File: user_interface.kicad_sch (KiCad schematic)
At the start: 33 parts, among them J3 Внутр. коннектор потенциометр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, J4 Внутр. коннектор галлетника (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, SW1 Кнопка тактовая 6x6 без фикса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, SW2 Кнопка тактовая 6x6 без фикса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, SW3 Кнопка тактовая 6x6 без фикса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, SW4 Кнопка тактовая 6x6 без фикса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, SW5 Кнопка тактовая 6x6 без фикса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, SW6 Кнопка тактовая 6x6 без фикса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

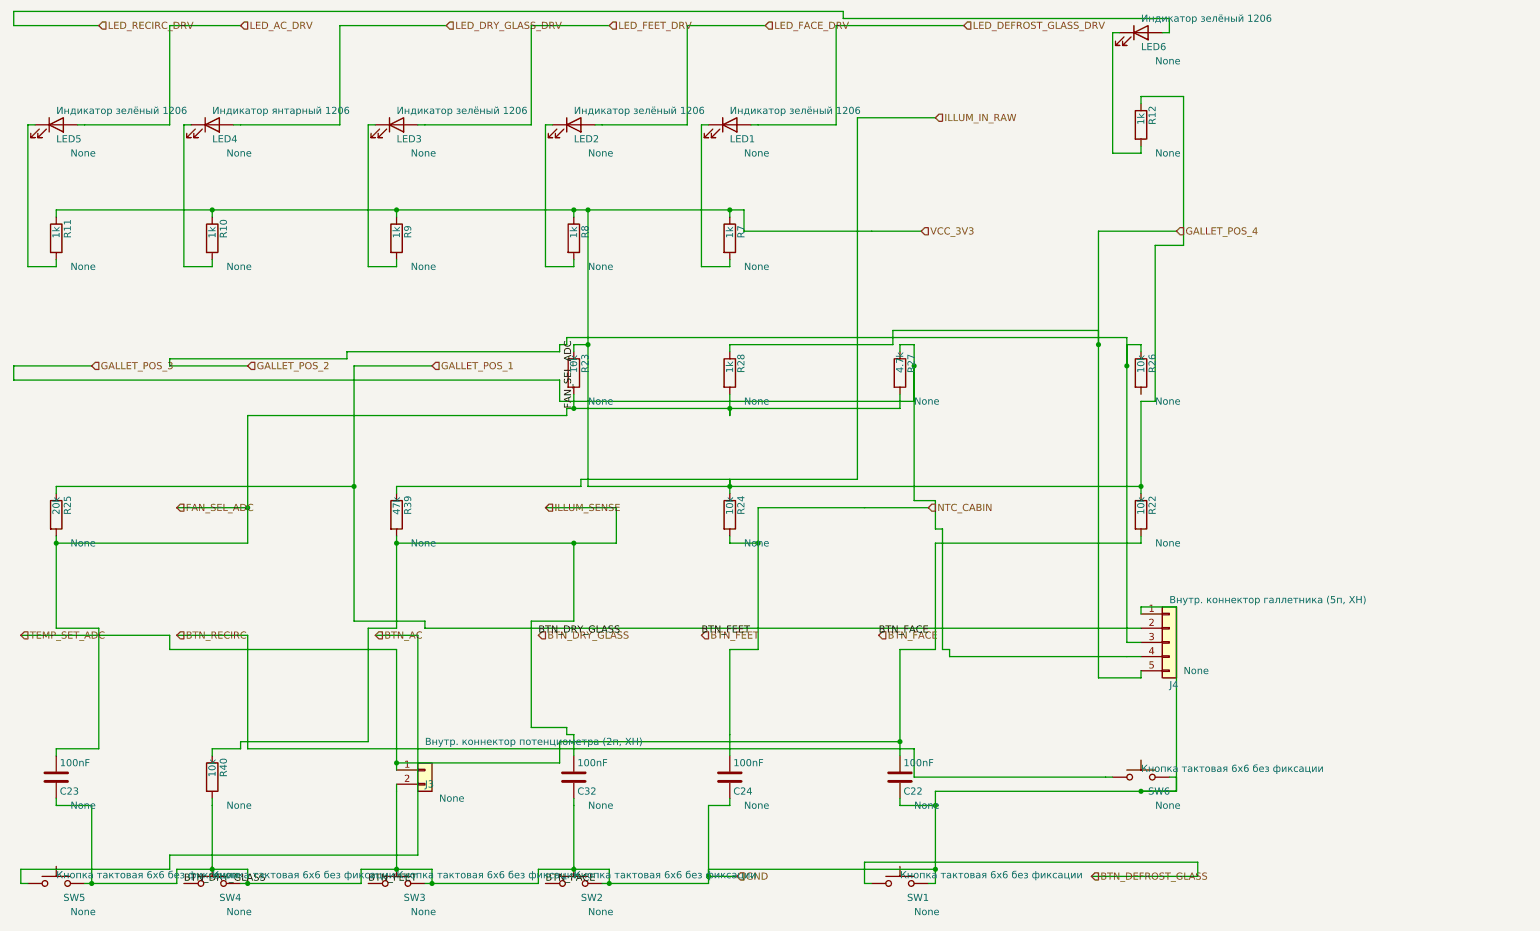
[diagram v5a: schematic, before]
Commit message: реализована 2я занятость клетки
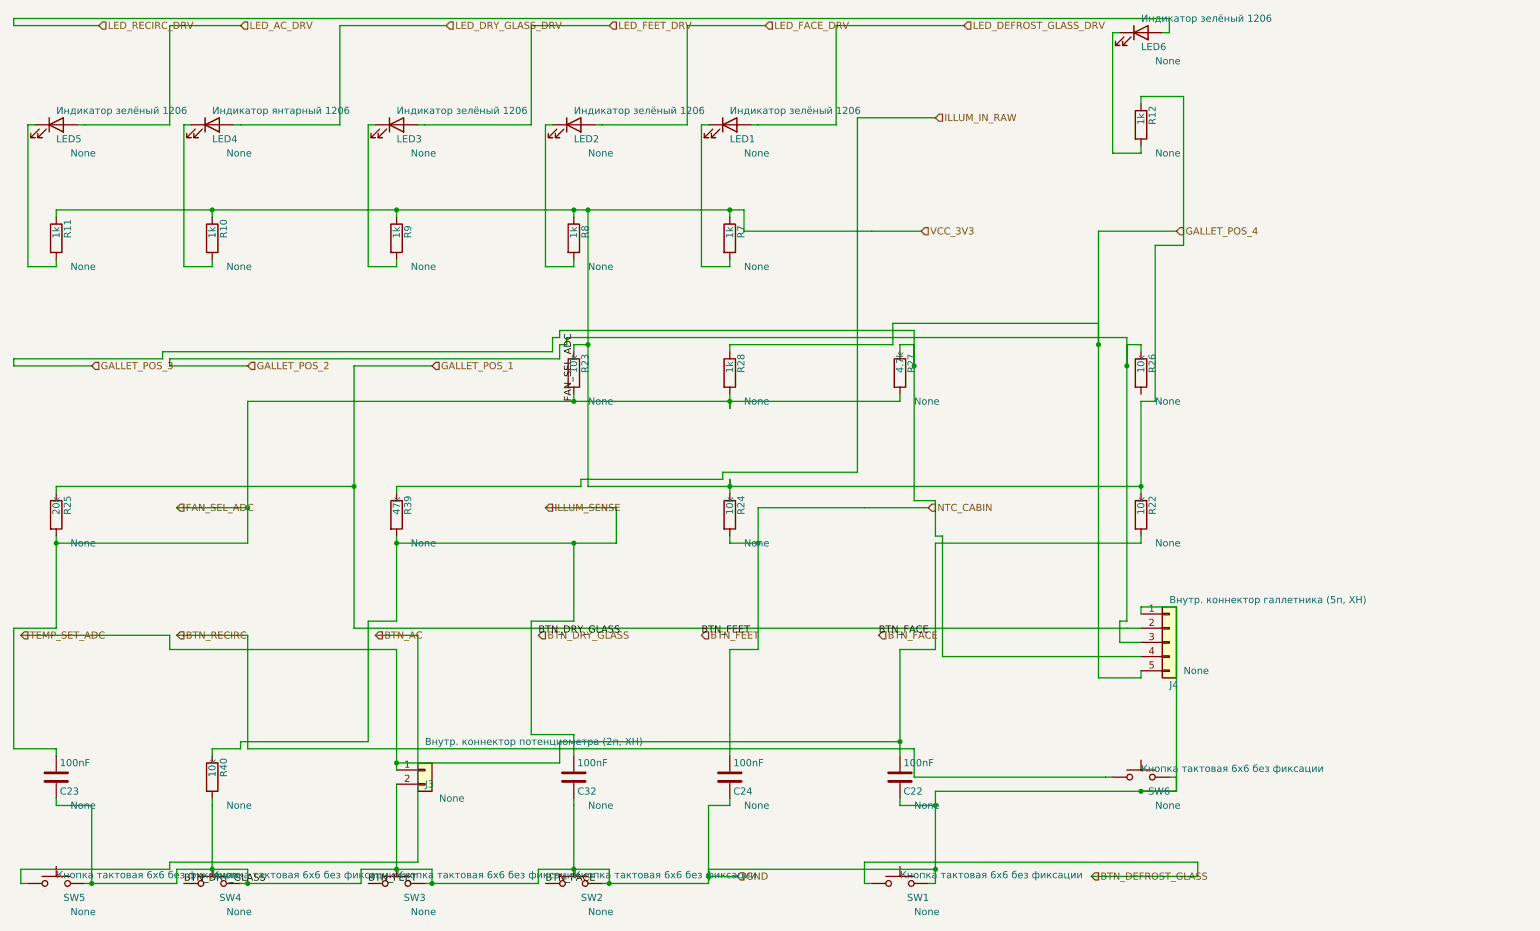
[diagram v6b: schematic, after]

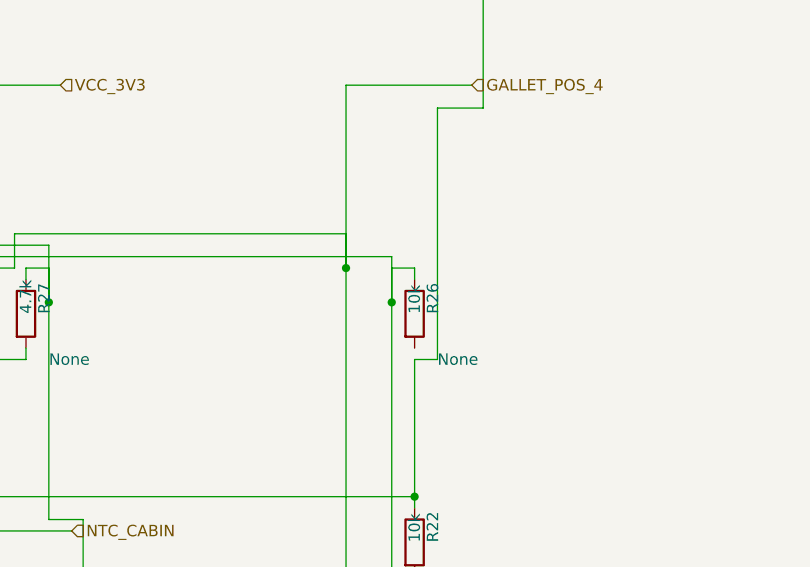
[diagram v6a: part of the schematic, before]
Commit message: фильтр клеток для Т если там пересечение
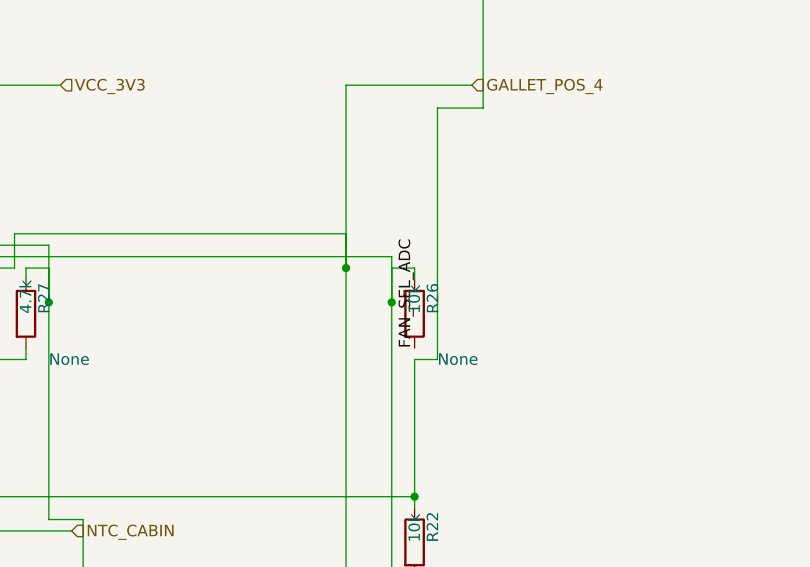
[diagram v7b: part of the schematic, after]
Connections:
- net FAN_SEL_ADC: now also R26.2
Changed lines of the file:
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@@
 		(instances
 			(project "Untitled"
-				(path "/80450f1d-307b-487e-a667-f10d610ada31"
+				(path "/5dda3bb2-7169-4d21-8754-437af9eafa82"
 					(reference "C22")
 					(unit 1)
@@
 		(instances
 			(project "Untitled"
-				(path "/80450f1d-307b-487e-a667-f10d610ada31"
+				(path "/5dda3bb2-7169-4d21-8754-437af9eafa82"
 					(reference "C23")
 					(unit 1)
@@
 		(instances
 			(project "Untitled"
-				(path "/80450f1d-307b-487e-a667-f10d610ada31"
+				(path "/5dda3bb2-7169-4d21-8754-437af9eafa82"
 					(reference "C24")
 					(unit 1)
@@
 		(instances
 			(project "Untitled"
-				(path "/80450f1d-307b-487e-a667-f10d610ada31"
+				(path "/5dda3bb2-7169-4d21-8754-437af9eafa82"
 					(reference "C32")
 					(unit 1)
@@
 		(instances
 			(project "Untitled"
-				(path "/80450f1d-307b-487e-a667-f10d610ada31"
+				(path "/5dda3bb2-7169-4d21-8754-437af9eafa82"
 					(reference "J3")
 					(unit 1)
@@
 		(instances
 			(project "Untitled"
-				(path "/80450f1d-307b-487e-a667-f10d610ada31"
+				(path "/5dda3bb2-7169-4d21-8754-437af9eafa82"
 					(reference "J4")
 					(unit 1)
@@
 		(instances
 			(project "Untitled"
-				(path "/80450f1d-307b-487e-a667-f10d610ada31"
+				(path "/5dda3bb2-7169-4d21-8754-437af9eafa82"
 					(reference "LED1")
 					(unit 1)
@@
 		(instances
 			(project "Untitled"
-				(path "/80450f1d-307b-487e-a667-f10d610ada31"
+				(path "/5dda3bb2-7169-4d21-8754-437af9eafa82"
 					(reference "LED2")
 					(unit 1)
@@
 		(instances
 			(project "Untitled"
-				(path "/80450f1d-307b-487e-a667-f10d610ada31"
+				(path "/5dda3bb2-7169-4d21-8754-437af9eafa82"
 					(reference "LED3")
 					(unit 1)
@@
 		(instances
 			(project "Untitled"
-				(path "/80450f1d-307b-487e-a667-f10d610ada31"
+				(path "/5dda3bb2-7169-4d21-8754-437af9eafa82"
 					(reference "LED4")
 					(unit 1)
@@
 		(instances
 			(project "Untitled"
-				(path "/80450f1d-307b-487e-a667-f10d610ada31"
+				(path "/5dda3bb2-7169-4d21-8754-437af9eafa82"
 					(reference "LED5")
 					(unit 1)
@@
 		(instances
 			(project "Untitled"
-				(path "/80450f1d-307b-487e-a667-f10d610ada31"
+				(path "/5dda3bb2-7169-4d21-8754-437af9eafa82"
 					(reference "LED6")
 					(unit 1)
@@
 		(instances
 			(project "Untitled"
-				(path "/80450f1d-307b-487e-a667-f10d610ada31"
+				(path "/5dda3bb2-7169-4d21-8754-437af9eafa82"
 					(reference "R7")
 					(unit 1)
@@
 		(instances
 			(project "Untitled"
-				(path "/80450f1d-307b-487e-a667-f10d610ada31"
+				(path "/5dda3bb2-7169-4d21-8754-437af9eafa82"
 					(reference "R8")
 					(unit 1)
@@
 		(instances
 			(project "Untitled"
-				(path "/80450f1d-307b-487e-a667-f10d610ada31"
+				(path "/5dda3bb2-7169-4d21-8754-437af9eafa82"
 					(reference "R9")
 					(unit 1)
@@
 		(instances
 			(project "Untitled"
-				(path "/80450f1d-307b-487e-a667-f10d610ada31"
+				(path "/5dda3bb2-7169-4d21-8754-437af9eafa82"
 					(reference "R10")
 					(unit 1)
@@
 		(instances
 			(project "Untitled"
-				(path "/80450f1d-307b-487e-a667-f10d610ada31"
+				(path "/5dda3bb2-7169-4d21-8754-437af9eafa82"
 					(reference "R11")
 					(unit 1)
@@
 		(instances
 			(project "Untitled"
-				(path "/80450f1d-307b-487e-a667-f10d610ada31"
+				(path "/5dda3bb2-7169-4d21-8754-437af9eafa82"
 					(reference "R12")
 					(unit 1)
@@
 		(instances
 			(project "Untitled"
-				(path "/80450f1d-307b-487e-a667-f10d610ada31"
+				(path "/5dda3bb2-7169-4d21-8754-437af9eafa82"
 					(reference "R22")
 					(unit 1)
@@
 		(instances
 			(project "Untitled"
-				(path "/80450f1d-307b-487e-a667-f10d610ada31"
+				(path "/5dda3bb2-7169-4d21-8754-437af9eafa82"
 					(reference "R23")
 					(unit 1)
@@
 		(instances
 			(project "Untitled"
-				(path "/80450f1d-307b-487e-a667-f10d610ada31"
+				(path "/5dda3bb2-7169-4d21-8754-437af9eafa82"
 					(reference "R24")
 					(unit 1)
@@
 		(instances
 			(project "Untitled"
-				(path "/80450f1d-307b-487e-a667-f10d610ada31"
+				(path "/5dda3bb2-7169-4d21-8754-437af9eafa82"
 					(reference "R39")
 					(unit 1)
@@
 		(instances
 			(project "Untitled"
-				(path "/80450f1d-307b-487e-a667-f10d610ada31"
+				(path "/5dda3bb2-7169-4d21-8754-437af9eafa82"
 					(reference "R40")
 					(unit 1)
@@
 		(instances
 			(project "Untitled"
-				(path "/80450f1d-307b-487e-a667-f10d610ada31"
+				(path "/5dda3bb2-7169-4d21-8754-437af9eafa82"
 					(reference "R25")
 					(unit 1)
@@
 		(instances
 			(project "Untitled"
-				(path "/80450f1d-307b-487e-a667-f10d610ada31"
+				(path "/5dda3bb2-7169-4d21-8754-437af9eafa82"
 					(reference "R26")
 					(unit 1)
@@
 		(instances
 			(project "Untitled"
-				(path "/80450f1d-307b-487e-a667-f10d610ada31"
+				(path "/5dda3bb2-7169-4d21-8754-437af9eafa82"
 					(reference "R27")
 					(unit 1)
@@
 		(instances
 			(project "Untitled"
-				(path "/80450f1d-307b-487e-a667-f10d610ada31"
+				(path "/5dda3bb2-7169-4d21-8754-437af9eafa82"
 					(reference "R28")
 					(unit 1)
@@
 		(instances
 			(project "Untitled"
-				(path "/80450f1d-307b-487e-a667-f10d610ada31"
+				(path "/5dda3bb2-7169-4d21-8754-437af9eafa82"
 					(reference "SW1")
 					(unit 1)
@@
 		(instances
 			(project "Untitled"
-				(path "/80450f1d-307b-487e-a667-f10d610ada31"
+				(path "/5dda3bb2-7169-4d21-8754-437af9eafa82"
 					(reference "SW2")
 					(unit 1)
@@
 		(instances
 			(project "Untitled"
-				(path "/80450f1d-307b-487e-a667-f10d610ada31"
+				(path "/5dda3bb2-7169-4d21-8754-437af9eafa82"
 					(reference "SW3")
 					(unit 1)
@@
 		(instances
 			(project "Untitled"
-				(path "/80450f1d-307b-487e-a667-f10d610ada31"
+				(path "/5dda3bb2-7169-4d21-8754-437af9eafa82"
 					(reference "SW4")
 					(unit 1)
@@
 		(instances
 			(project "Untitled"
-				(path "/80450f1d-307b-487e-a667-f10d610ada31"
+				(path "/5dda3bb2-7169-4d21-8754-437af9eafa82"
 					(reference "SW5")
 					(unit 1)
@@
 		(instances
 			(project "Untitled"
-				(path "/80450f1d-307b-487e-a667-f10d610ada31"
+				(path "/5dda3bb2-7169-4d21-8754-437af9eafa82"
 					(reference "SW6")
 					(unit 1)
@@
 		(effects
 			(font
+				(size 1.27 1.27)
+			)
+			(justify left bottom)
+		)
+	)
+	(label "FAN_SEL_ADC"
+		(at 204.47 69.85 270)
+		(effects
+			(font

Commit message: fic placer for small schemes
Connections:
- net LED_FACE_A: now reaches LED2.1 (K), R8.2
- net LED_FEET_A: now reaches LED3.1 (K), R9.2
- net LED_DEFROST_GLASS_A: now reaches LED1.1 (K), R7.2
- net LED_DRY_GLASS_A: now reaches LED4.1 (K), R10.2
- net LED_RECIRC_A: now reaches LED6.1 (K), R12.2
- net LED_AC_A: now reaches LED5.1 (K), R11.2
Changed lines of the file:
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@@
 		(instances
 			(project "Untitled"
-				(path "/5dda3bb2-7169-4d21-8754-437af9eafa82"
+				(path "/f6aca846-33e6-4903-9ab4-0f8f6bf1ede3"
 					(reference "C22")
 					(unit 1)
@@
 		(instances
 			(project "Untitled"
-				(path "/5dda3bb2-7169-4d21-8754-437af9eafa82"
+				(path "/f6aca846-33e6-4903-9ab4-0f8f6bf1ede3"
 					(reference "C23")
 					(unit 1)
@@
 		(instances
 			(project "Untitled"
-				(path "/5dda3bb2-7169-4d21-8754-437af9eafa82"
+				(path "/f6aca846-33e6-4903-9ab4-0f8f6bf1ede3"
 					(reference "C24")
 					(unit 1)
@@
 		(instances
 			(project "Untitled"
-				(path "/5dda3bb2-7169-4d21-8754-437af9eafa82"
+				(path "/f6aca846-33e6-4903-9ab4-0f8f6bf1ede3"
 					(reference "C32")
 					(unit 1)
@@
 		(instances
 			(project "Untitled"
-				(path "/5dda3bb2-7169-4d21-8754-437af9eafa82"
+				(path "/f6aca846-33e6-4903-9ab4-0f8f6bf1ede3"
 					(reference "J3")
 					(unit 1)
@@
 		(instances
 			(project "Untitled"
-				(path "/5dda3bb2-7169-4d21-8754-437af9eafa82"
+				(path "/f6aca846-33e6-4903-9ab4-0f8f6bf1ede3"
 					(reference "J4")
 					(unit 1)
@@
 		(instances
 			(project "Untitled"
-				(path "/5dda3bb2-7169-4d21-8754-437af9eafa82"
+				(path "/f6aca846-33e6-4903-9ab4-0f8f6bf1ede3"
 					(reference "LED1")
 					(unit 1)
@@
 		(instances
 			(project "Untitled"
-				(path "/5dda3bb2-7169-4d21-8754-437af9eafa82"
+				(path "/f6aca846-33e6-4903-9ab4-0f8f6bf1ede3"
 					(reference "LED2")
 					(unit 1)
@@
 		(instances
 			(project "Untitled"
-				(path "/5dda3bb2-7169-4d21-8754-437af9eafa82"
+				(path "/f6aca846-33e6-4903-9ab4-0f8f6bf1ede3"
 					(reference "LED3")
 					(unit 1)
@@
 		(instances
 			(project "Untitled"
-				(path "/5dda3bb2-7169-4d21-8754-437af9eafa82"
+				(path "/f6aca846-33e6-4903-9ab4-0f8f6bf1ede3"
 					(reference "LED4")
 					(unit 1)
@@
 		(instances
 			(project "Untitled"
-				(path "/5dda3bb2-7169-4d21-8754-437af9eafa82"
+				(path "/f6aca846-33e6-4903-9ab4-0f8f6bf1ede3"
 					(reference "LED5")
 					(unit 1)
@@
 		(instances
 			(project "Untitled"
-				(path "/5dda3bb2-7169-4d21-8754-437af9eafa82"
+				(path "/f6aca846-33e6-4903-9ab4-0f8f6bf1ede3"
 					(reference "LED6")
 					(unit 1)
@@
 		(instances
 			(project "Untitled"
-				(path "/5dda3bb2-7169-4d21-8754-437af9eafa82"
+				(path "/f6aca846-33e6-4903-9ab4-0f8f6bf1ede3"
 					(reference "R7")
 					(unit 1)
@@
 		(instances
 			(project "Untitled"
-				(path "/5dda3bb2-7169-4d21-8754-437af9eafa82"
+				(path "/f6aca846-33e6-4903-9ab4-0f8f6bf1ede3"
 					(reference "R8")
 					(unit 1)
@@
 		(instances
 			(project "Untitled"
-				(path "/5dda3bb2-7169-4d21-8754-437af9eafa82"
+				(path "/f6aca846-33e6-4903-9ab4-0f8f6bf1ede3"
 					(reference "R9")
 					(unit 1)
@@
 		(instances
 			(project "Untitled"
-				(path "/5dda3bb2-7169-4d21-8754-437af9eafa82"
+				(path "/f6aca846-33e6-4903-9ab4-0f8f6bf1ede3"
 					(reference "R10")
 					(unit 1)
@@
 		(instances
 			(project "Untitled"
-				(path "/5dda3bb2-7169-4d21-8754-437af9eafa82"
+				(path "/f6aca846-33e6-4903-9ab4-0f8f6bf1ede3"
 					(reference "R11")
 					(unit 1)
@@
 		(instances
 			(project "Untitled"
-				(path "/5dda3bb2-7169-4d21-8754-437af9eafa82"
+				(path "/f6aca846-33e6-4903-9ab4-0f8f6bf1ede3"
 					(reference "R12")
 					(unit 1)
@@
 		(instances
 			(project "Untitled"
-				(path "/5dda3bb2-7169-4d21-8754-437af9eafa82"
+				(path "/f6aca846-33e6-4903-9ab4-0f8f6bf1ede3"
 					(reference "R22")
 					(unit 1)
@@
 		(instances
 			(project "Untitled"
-				(path "/5dda3bb2-7169-4d21-8754-437af9eafa82"
+				(path "/f6aca846-33e6-4903-9ab4-0f8f6bf1ede3"
 					(reference "R23")
 					(unit 1)
@@
 		(instances
 			(project "Untitled"
-				(path "/5dda3bb2-7169-4d21-8754-437af9eafa82"
+				(path "/f6aca846-33e6-4903-9ab4-0f8f6bf1ede3"
 					(reference "R24")
 					(unit 1)
@@
 		(instances
 			(project "Untitled"
-				(path "/5dda3bb2-7169-4d21-8754-437af9eafa82"
+				(path "/f6aca846-33e6-4903-9ab4-0f8f6bf1ede3"
 					(reference "R39")
 					(unit 1)
@@
 		(instances
 			(project "Untitled"
-				(path "/5dda3bb2-7169-4d21-8754-437af9eafa82"
+				(path "/f6aca846-33e6-4903-9ab4-0f8f6bf1ede3"
 					(reference "R40")
 					(unit 1)
@@
 		(instances
 			(project "Untitled"
-				(path "/5dda3bb2-7169-4d21-8754-437af9eafa82"
+				(path "/f6aca846-33e6-4903-9ab4-0f8f6bf1ede3"
 					(reference "R25")
 					(unit 1)
@@
 		(instances
 			(project "Untitled"
-				(path "/5dda3bb2-7169-4d21-8754-437af9eafa82"
+				(path "/f6aca846-33e6-4903-9ab4-0f8f6bf1ede3"
 					(reference "R26")
 					(unit 1)
@@
 		(instances
 			(project "Untitled"
-				(path "/5dda3bb2-7169-4d21-8754-437af9eafa82"
+				(path "/f6aca846-33e6-4903-9ab4-0f8f6bf1ede3"
 					(reference "R27")
 					(unit 1)
@@
 		(instances
 			(project "Untitled"
-				(path "/5dda3bb2-7169-4d21-8754-437af9eafa82"
+				(path "/f6aca846-33e6-4903-9ab4-0f8f6bf1ede3"
 					(reference "R28")
 					(unit 1)
@@
 		(instances
 			(project "Untitled"
-				(path "/5dda3bb2-7169-4d21-8754-437af9eafa82"
+				(path "/f6aca846-33e6-4903-9ab4-0f8f6bf1ede3"
 					(reference "SW1")
 					(unit 1)
@@
 		(instances
 			(project "Untitled"
-				(path "/5dda3bb2-7169-4d21-8754-437af9eafa82"
+				(path "/f6aca846-33e6-4903-9ab4-0f8f6bf1ede3"
 					(reference "SW2")
 					(unit 1)
@@
 		(instances
 			(project "Untitled"
-				(path "/5dda3bb2-7169-4d21-8754-437af9eafa82"
+				(path "/f6aca846-33e6-4903-9ab4-0f8f6bf1ede3"
 					(reference "SW3")
 					(unit 1)
@@
 		(instances
 			(project "Untitled"
-				(path "/5dda3bb2-7169-4d21-8754-437af9eafa82"
+				(path "/f6aca846-33e6-4903-9ab4-0f8f6bf1ede3"
 					(reference "SW4")
 					(unit 1)
@@
 		(instances
 			(project "Untitled"
-				(path "/5dda3bb2-7169-4d21-8754-437af9eafa82"
+				(path "/f6aca846-33e6-4903-9ab4-0f8f6bf1ede3"
 					(reference "SW5")
 					(unit 1)
@@
 		(instances
 			(project "Untitled"
-				(path "/5dda3bb2-7169-4d21-8754-437af9eafa82"
+				(path "/f6aca846-33e6-4903-9ab4-0f8f6bf1ede3"
 					(reference "SW6")
 					(unit 1)
@@
 		(effects
 			(font
+				(size 1.27 1.27)
+			)
+			(justify left bottom)
+		)
+	)
+	(label "LED_DEFROST_GLASS_A"
+		(at 128.27 46.99 270)
+		(effects
+			(font
+				(size 1.27 1.27)
+			)
+			(justify left bottom)
+		)
+	)
+	(label "LED_FACE_A"
+		(at 100.33 46.99 270)
+		(effects
+			(font
+				(size 1.27 1.27)
+			)
+			(justify left bottom)
+		)
+	)
+	(label "LED_FEET_A"
+		(at 68.58 46.99 270)
+		(effects
+			(font
+				(size 1.27 1.27)
+			)
+			(justify left bottom)
+		)
+	)
+	(label "LED_DRY_GLASS_A"
+		(at 35.56 46.99 270)
+		(effects
+			(font
+				(size 1.27 1.27)
+			)
+			(justify left bottom)
+		)
+	)
+	(label "LED_AC_A"
+		(at 7.62 46.99 270)
+		(effects
+			(font
+				(size 1.27 1.27)
+			)
+			(justify left bottom)
+		)
+	)
+	(label "LED_RECIRC_A"
+		(at 201.93 26.67 270)
+		(effects
+			(font
